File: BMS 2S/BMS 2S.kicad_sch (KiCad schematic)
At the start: 1 part

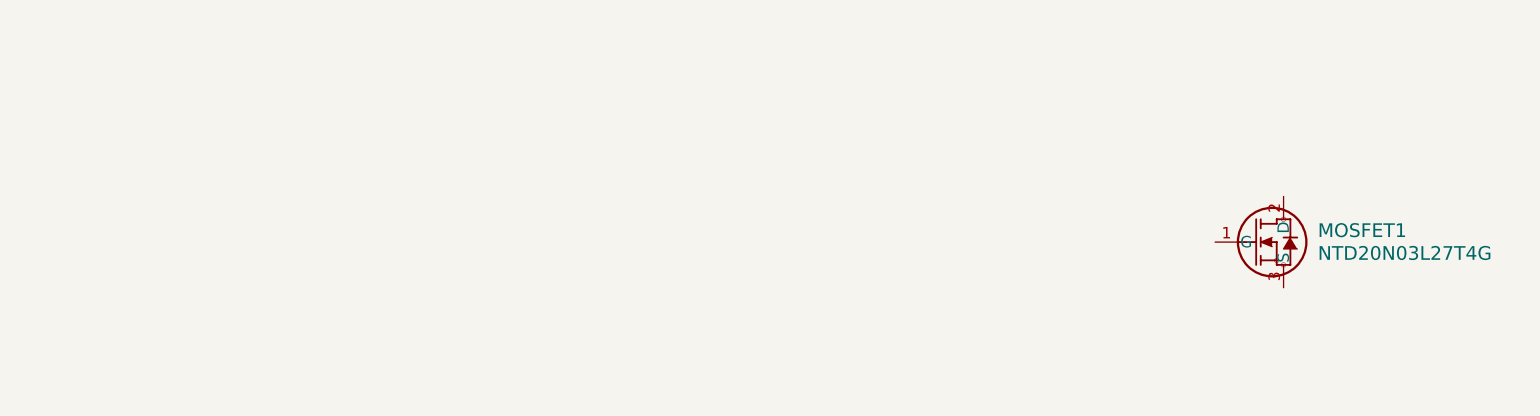
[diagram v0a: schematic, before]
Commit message: BMS 2S
Schéma et début de l'esquisse du pcb
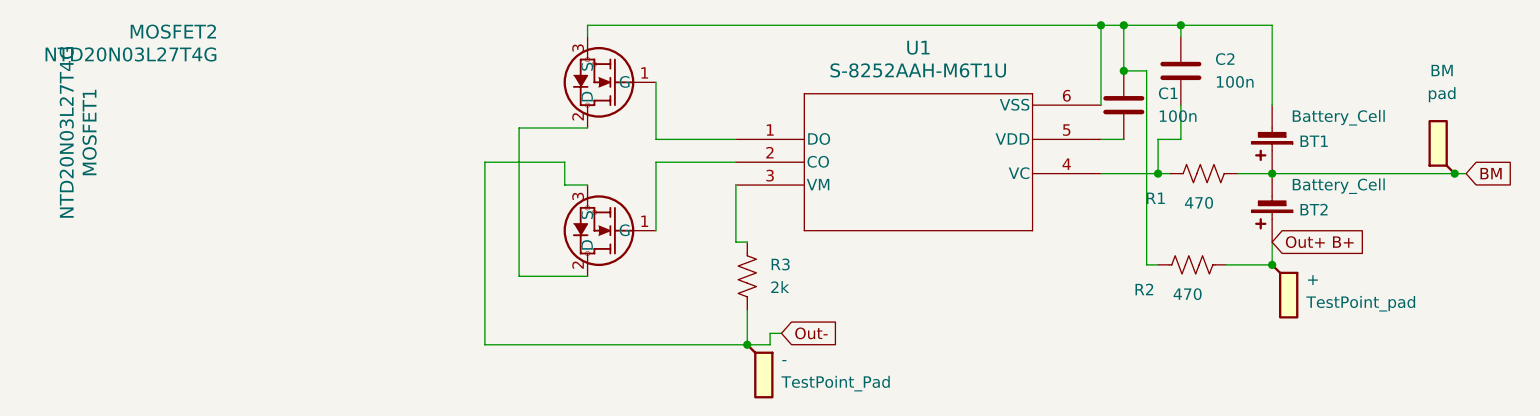
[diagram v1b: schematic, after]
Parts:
- added +: TestPoint_pad, symbol Connector:TestPoint_Flag
- added -: TestPoint_Pad, symbol Connector:TestPoint_Flag
- added BM: pad, symbol Connector:TestPoint_Flag
- added BT1, BT2: Battery_Cell, symbol Device:Battery_Cell
- added C1, C2: 100n, symbol Device:C
- added MOSFET2: NTD20N03L27T4G, DPAK_369C_ONS, symbol 2025-12-30_20-21-14:NTD20N03L27T4G
- added R1, R2: 470, symbol Device:R_US
- added R3: 2k, symbol Device:R_US
- added U1: S-8252AAH-M6T1U, SOT236-A-PKG_MP006-A-P-SD-2.1_ABL, symbol BMS_sym:S-8252AAH-M6T1U
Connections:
- net at MOSFET1.1 (G): now also U1.2 (CO)
- net at MOSFET1.2 (D): now also MOSFET2.2 (D)
- net Out-: now reaches MOSFET1.3 (S)
- net Out-: now also -.1, R3.2
- new net: MOSFET2.1 (G), U1.1 (DO)
- new net: R3.1, U1.3 (VM)
- new net: C2.2, R1.1, U1.4 (VC)
- new net: C1.2, U1.5 (VDD)
- new net: BT1.2 (-), C1.1, C2.1, MOSFET2.3 (S), R2.1, U1.6 (VSS)
- new net BM: BM.1, BT1.1 (+), BT2.2 (-), R1.2
- new net Out+ B+: +.1, BT2.1 (+), R2.2
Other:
- moved on the sheet: MOSFET1
